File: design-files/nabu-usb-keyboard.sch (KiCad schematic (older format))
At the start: 12 parts, among them J1 Console UART header, J2 Debug Event Header, J3 DIN-6, J4 9V input, Q1 SiHLU110-GE3, U1 74LVC245, U2 Pico, U3 SN75176AP

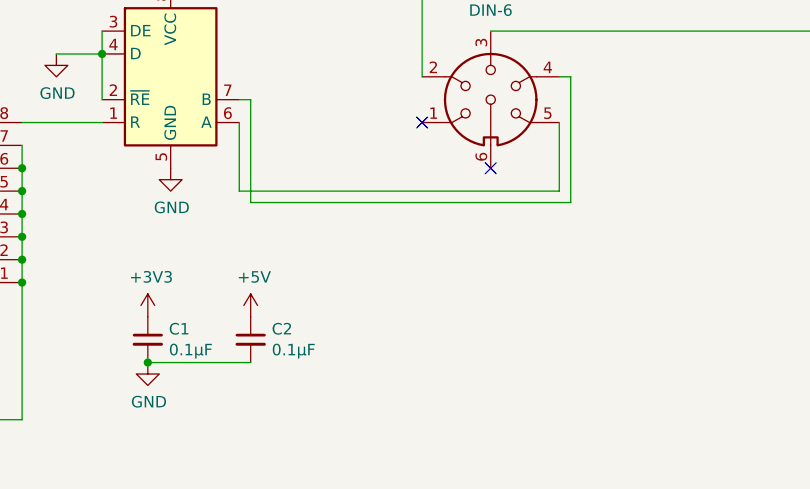
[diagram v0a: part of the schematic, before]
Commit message: De-glitch the RS422 input in the same fashion as the NABU.
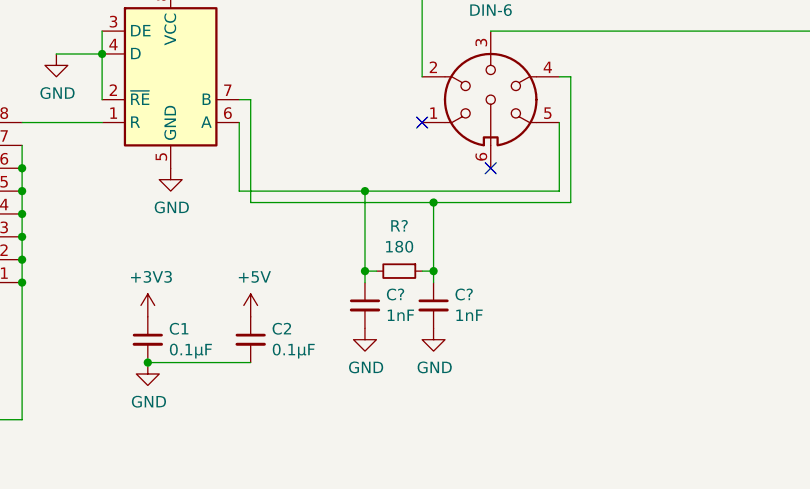
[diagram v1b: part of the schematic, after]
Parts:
- added C? (x2): 1nF, symbol Device:C_Small
- added R?: 180, Resistor_THT:R_Axial_DIN0207_L6.3mm_D2.5mm_P2.54mm_Vertical, symbol Device:R_Small
- R1: footprint Resistor_THT:R_Axial_DIN0204_L3.6mm_D1.6mm_P5.08mm_Horizontal -> Resistor_THT:R_Axial_DIN0207_L6.3mm_D2.5mm_P7.62mm_Horizontal; Part (none) -> YAGEO MFR50SFTE52-10K
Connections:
- net GND: now also C?.2, C?.2
- net at J3.5, U3.6 (A): now also C?.1, R?.2
- net at J3.4, U3.7 (B): now also C?.1, R?.1
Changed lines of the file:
@@
 F 0 "R1" H 8000 2550 50  0000 L CNN
 F 1 "10K" H 7950 2450 50  0000 L CNN
-F 2 "Resistor_THT:R_Axial_DIN0204_L3.6mm_D1.6mm_P5.08mm_Horizontal" H 8150 2500 50  0001 C CNN
+F 2 "Resistor_THT:R_Axial_DIN0207_L6.3mm_D2.5mm_P7.62mm_Horizontal" H 8150 2500 50  0001 C CNN
 F 3 "~" H 8150 2500 50  0001 C CNN
+F 4 "YAGEO MFR50SFTE52-10K" H 8150 2500 50  0001 C CNN "Part"
 	1    8150 2500
 	1    0    0    -1
@@
 	5900 4900 5900 5200
 Wire Wire Line
-	5900 5200 7300 5200
+	5900 5200 6450 5200
 Wire Wire Line
 	7300 5200 7300 4900
@@
 	5950 4800 5950 5250
 Wire Wire Line
-	5950 5250 7350 5250
+	5950 5250 6750 5250
 Wire Wire Line
 	7350 5250 7350 4700
@@
 	8450 2100 8450 2200
 Connection ~ 8450 2200
+$Comp
+L Device:R_Small R?
+U 1 1 63A06755
+P 6600 5550
+F 0 "R?" V 6404 5550 50  0000 C CNN
+F 1 "180" V 6495 5550 50  0000 C CNN
+F 2 "Resistor_THT:R_Axial_DIN0207_L6.3mm_D2.5mm_P2.54mm_Vertical" H 6600 5550 50  0001 C CNN
+F 3 "~" H 6600 5550 50  0001 C CNN
+F 4 "YAGEO MFR50SFTE52-180R" V 6600 5550 50  0001 C CNN "Part"
+	1    6600 5550
+	0    1    1    0
+$EndComp
+Wire Wire Line
+	6450 5600 6450 5550
+Connection ~ 6450 5200
+Wire Wire Line
+	6450 5200 7300 5200
+Wire Wire Line
+	6750 5600 6750 5550
+Connection ~ 6750 5250
+Wire Wire Line
+	6750 5250 7350 5250
+Wire Wire Line
+	6700 5550 6750 5550
+Connection ~ 6750 5550
+Wire Wire Line
+	6750 5550 6750 5250
+Wire Wire Line
+	6500 5550 6450 5550
+Connection ~ 6450 5550
+Wire Wire Line
+	6450 5550 6450 5200
+$Comp
+L power:GND #PWR?
+U 1 1 63A0CAA3
+P 6750 5800
+F 0 "#PWR?" H 6750 5550 50  0001 C CNN
+F 1 "GND" H 6755 5627 50  0000 C CNN
+F 2 "" H 6750 5800 50  0001 C CNN
+F 3 "" H 6750 5800 50  0001 C CNN
+	1    6750 5800
+	1    0    0    -1
+$EndComp
+$Comp
+L power:GND #PWR?
+U 1 1 63A11E4C
+P 6450 5800
+F 0 "#PWR?" H 6450 5550 50  0001 C CNN
+F 1 "GND" H 6455 5627 50  0000 C CNN
+F 2 "" H 6450 5800 50  0001 C CNN
+F 3 "" H 6450 5800 50  0001 C CNN
+	1    6450 5800
+	1    0    0    -1
+$EndComp
+$Comp
+L Device:C_Small C?
+U 1 1 63A12AC5
+P 6450 5700
+F 0 "C?" H 6542 5746 50  0000 L CNN
+F 1 "1nF" H 6542 5655 50  0000 L CNN
+F 2 "" H 6450 5700 50  0001 C CNN
+F 3 "~" H 6450 5700 50  0001 C CNN
+	1    6450 5700
+	1    0    0    -1
+$EndComp
+$Comp
+L Device:C_Small C?
+U 1 1 63A131AF
+P 6750 5700
+F 0 "C?" H 6842 5746 50  0000 L CNN
+F 1 "1nF" H 6842 5655 50  0000 L CNN
+F 2 "" H 6750 5700 50  0001 C CNN
+F 3 "~" H 6750 5700 50  0001 C CNN
+	1    6750 5700
+	1    0    0    -1
+$EndComp
 $EndSCHEMATC

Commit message: Finalize the first prototype PCB.
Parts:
- removed J2: Debug Event Header, Connector_PinHeader_2.54mm:PinHeader_1x03_P2.54mm_Vertical, symbol Connector:Conn_01x03_Male
- added D1: 1N4001, Diode_THT:D_DO-41_SOD81_P10.16mm_Horizontal, symbol Diode:1N4001
- C1, C2: footprint Capacitor_THT:C_Disc_D5.0mm_W2.5mm_P5.00mm -> Capacitor_THT:C_Disc_D6.0mm_W4.4mm_P5.00mm
- C3, C4: renamed from C?; footprint (none) -> Capacitor_THT:C_Disc_D6.0mm_W4.4mm_P5.00mm
- J2: renamed from J3; footprint Connector_PinHeader_2.54mm:PinHeader_1x06_P2.54mm_Horizontal -> jrt-Connectors:Jack_DIN-6_CLIFF_FC680806
- J3: renamed from J4; footprint Connector_BarrelJack:BarrelJack_CUI_PJ-102AH_Horizontal -> jrt-Connectors:Kobiconn_163-179PH-EX-5_5-2_1mm-1_5A
- Q1: value SiHLU110-GE3 -> IRLU110PBF
- gave numbers to parts that had none: 1
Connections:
- net +9V: now also D1.2 (A); no longer J2.3
- new net: D1.1 (K), J2.3
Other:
- note removed: "C"
- note removed: "V"
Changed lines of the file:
@@
 Sheet 1 1
 Title "NABU Keyboard to USB Adapter"
-Date "2022-12-13"
+Date "2022-12-19"
 Rev "0.1"
 Comp "(c) 2022 Jason R. Thorpe. See LICENSE."
@@
 F 0 "C1" H 5592 5896 50  0000 L CNN
 F 1 "0.1µF" H 5592 5805 50  0000 L CNN
-F 2 "Capacitor_THT:C_Disc_D5.0mm_W2.5mm_P5.00mm" H 5500 5850 50  0001 C CNN
+F 2 "Capacitor_THT:C_Disc_D6.0mm_W4.4mm_P5.00mm" H 5500 5850 50  0001 C CNN
 F 3 "~" H 5500 5850 50  0001 C CNN
 	1    5500 5850
@@
 F 0 "C2" H 6042 5896 50  0000 L CNN
 F 1 "0.1µF" H 6042 5805 50  0000 L CNN
-F 2 "Capacitor_THT:C_Disc_D5.0mm_W2.5mm_P5.00mm" H 5950 5850 50  0001 C CNN
+F 2 "Capacitor_THT:C_Disc_D6.0mm_W4.4mm_P5.00mm" H 5950 5850 50  0001 C CNN
 F 3 "~" H 5950 5850 50  0001 C CNN
 	1    5950 5850
@@
 	0    1    1    0
 $EndComp
-$Comp
-L Connector:Conn_01x03_Male J2
-U 1 1 639B268F
-P 7300 3300
-F 0 "J2" H 7408 3581 50  0000 C CNN
-F 1 "Debug Event Header" H 7400 3500 50  0000 C CNN
-F 2 "Connector_PinHeader_2.54mm:PinHeader_1x03_P2.54mm_Vertical" H 7300 3300 50  0001 C CNN
-F 3 "~" H 7300 3300 50  0001 C CNN
-	1    7300 3300
-	-1   0    0    -1
-$EndComp
-Text Notes 7350 3250 0    39   ~ 0
-GND
-Text Notes 7350 3350 0    39   ~ 0
-C
-Text Notes 7350 3450 0    39   ~ 0
-V
 Wire Wire Line
 	3500 2100 3500 4900
@@
 NoConn ~ 5700 3600
 $Comp
-L Connector:DIN-6 J3
+L Connector:DIN-6 J2
 U 1 1 639C63C6
 P 7000 4800
-F 0 "J3" H 7000 5281 50  0000 C CNN
+F 0 "J2" H 7000 5281 50  0000 C CNN
 F 1 "DIN-6" H 7000 5190 50  0000 C CNN
-F 2 "Connector_PinHeader_2.54mm:PinHeader_1x06_P2.54mm_Horizontal" H 7000 4800 50  0001 C CNN
+F 2 "jrt-Connectors:Jack_DIN-6_CLIFF_FC680806" H 7000 4800 50  0001 C CNN
 F 3 "https://datasheet.octopart.com/MAB-6-H-Hirschmann-datasheet-569838.pdf" H 7000 4800 50  0001 C CNN
 F 4 "" H 7000 4800 50  0001 C CNN "Field4"
@@
 $EndComp
 $Comp
-L Connector:Barrel_Jack_Switch J4
+L Connector:Barrel_Jack_Switch J3
 U 1 1 639C840A
 P 9550 2500
-F 0 "J4" H 9320 2542 50  0000 R CNN
+F 0 "J3" H 9320 2542 50  0000 R CNN
 F 1 "9V input" H 9320 2451 50  0000 R CNN
-F 2 "Connector_BarrelJack:BarrelJack_CUI_PJ-102AH_Horizontal" H 9600 2460 50  0001 C CNN
+F 2 "jrt-Connectors:Kobiconn_163-179PH-EX-5_5-2_1mm-1_5A" H 9600 2460 50  0001 C CNN
 F 3 "~" H 9600 2460 50  0001 C CNN
 	1    9550 2500
@@
 P 8350 2400
 F 0 "Q1" H 8554 2446 50  0000 L CNN
-F 1 "SiHLU110-GE3" H 8554 2355 50  0000 L CNN
+F 1 "IRLU110PBF" H 8554 2355 50  0000 L CNN
 F 2 "Package_TO_SOT_THT:TO-251-3-1EP_Horizontal_TabDown" H 8550 2500 50  0001 C CNN
 F 3 "~" H 8350 2400 50  0001 C CNN
@@
 	10250 2250 10250 4500
 Wire Wire Line
-	10250 4500 7000 4500
-Wire Wire Line
 	9250 2250 10250 2250
 Wire Wire Line
@@
 	10250 2250 10250 2050
 Connection ~ 10250 2250
-Wire Wire Line
-	6400 3200 7100 3200
-Connection ~ 6400 3200
-Wire Wire Line
-	6300 3300 7100 3300
-Wire Wire Line
-	6300 3400 7100 3400
 $Comp
 L power:GND #PWR0101
@@
 $EndComp
 Connection ~ 4800 3200
-$Comp
-L power:GND #PWR0102
-U 1 1 639D6425
-P 6400 1700
-F 0 "#PWR0102" H 6400 1450 50  0001 C CNN
-F 1 "GND" V 6405 1572 50  0000 R CNN
-F 2 "" H 6400 1700 50  0001 C CNN
-F 3 "" H 6400 1700 50  0001 C CNN
-	1    6400 1700
-	0    -1   -1   0
-$EndComp
-Connection ~ 6400 1700
 Text Label 8450 2100 0    50   ~ 0
 9VRET
@@
 Connection ~ 8450 2200
 $Comp
-L Device:R_Small R?
+L Device:R_Small R2
 U 1 1 63A06755
 P 6600 5550
-F 0 "R?" V 6404 5550 50  0000 C CNN
+F 0 "R2" V 6404 5550 50  0000 C CNN
 F 1 "180" V 6495 5550 50  0000 C CNN
 F 2 "Resistor_THT:R_Axial_DIN0207_L6.3mm_D2.5mm_P2.54mm_Vertical" H 6600 5550 50  0001 C CNN
@@
 	6450 5550 6450 5200
 $Comp
-L power:GND #PWR?
+L power:GND #PWR0103
 U 1 1 63A0CAA3
 P 6750 5800
-F 0 "#PWR?" H 6750 5550 50  0001 C CNN
+F 0 "#PWR0103" H 6750 5550 50  0001 C CNN
 F 1 "GND" H 6755 5627 50  0000 C CNN
 F 2 "" H 6750 5800 50  0001 C CNN
@@
 $EndComp
 $Comp
-L power:GND #PWR?
+L power:GND #PWR0104
 U 1 1 63A11E4C
 P 6450 5800
-F 0 "#PWR?" H 6450 5550 50  0001 C CNN
+F 0 "#PWR0104" H 6450 5550 50  0001 C CNN
 F 1 "GND" H 6455 5627 50  0000 C CNN
 F 2 "" H 6450 5800 50  0001 C CNN
@@
 $EndComp
 $Comp
-L Device:C_Small C?
+L Device:C_Small C3
 U 1 1 63A12AC5
 P 6450 5700
-F 0 "C?" H 6542 5746 50  0000 L CNN
+F 0 "C3" H 6542 5746 50  0000 L CNN
 F 1 "1nF" H 6542 5655 50  0000 L CNN
-F 2 "" H 6450 5700 50  0001 C CNN
+F 2 "Capacitor_THT:C_Disc_D6.0mm_W4.4mm_P5.00mm" H 6450 5700 50  0001 C CNN
 F 3 "~" H 6450 5700 50  0001 C CNN
 	1    6450 5700
@@
 $EndComp
 $Comp
-L Device:C_Small C?
+L Device:C_Small C4
 U 1 1 63A131AF
 P 6750 5700
-F 0 "C?" H 6842 5746 50  0000 L CNN
+F 0 "C4" H 6842 5746 50  0000 L CNN
 F 1 "1nF" H 6842 5655 50  0000 L CNN
-F 2 "" H 6750 5700 50  0001 C CNN
+F 2 "Capacitor_THT:C_Disc_D6.0mm_W4.4mm_P5.00mm" H 6750 5700 50  0001 C CNN
 F 3 "~" H 6750 5700 50  0001 C CNN
 	1    6750 5700
 	1    0    0    -1
 $EndComp
+$Comp
+L power:GND #PWR0102
+U 1 1 639D6425
+P 6400 3200
+F 0 "#PWR0102" H 6400 2950 50  0001 C CNN
+F 1 "GND" V 6405 3072 50  0000 R CNN
+F 2 "" H 6400 3200 50  0001 C CNN
+F 3 "" H 6400 3200 50  0001 C CNN
+	1    6400 3200
+	0    -1   -1   0
+$EndComp
+Connection ~ 6400 3200
+$Comp
+L Diode:1N4001 D1
+U 1 1 63A35253
+P 8950 4500
+F 0 "D1" H 8950 4300 50  0000 C CNN
+F 1 "1N4001" H 8950 4400 50  0000 C CNN
+F 2 "Diode_THT:D_DO-41_SOD81_P10.16mm_Horizontal" H 8950 4325 50  0001 C CNN
+F 3 "http://www.vishay.com/docs/88503/1n4001.pdf" H 8950 4500 50  0001 C CNN
+	1    8950 4500
+	1    0    0    -1
+$EndComp
+Wire Wire Line
+	10250 4500 9100 4500
+Wire Wire Line
+	8800 4500 7000 4500
 $EndSCHEMATC
